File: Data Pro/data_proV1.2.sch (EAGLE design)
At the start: 43 parts, among them IC1 4049N, IC2 MCP3008, IC3 OP11S, IC6 AT24CP, J1 RASPBERRYPI-40-PIN-GPIO, U1 DS18B20, X1 32.768khz

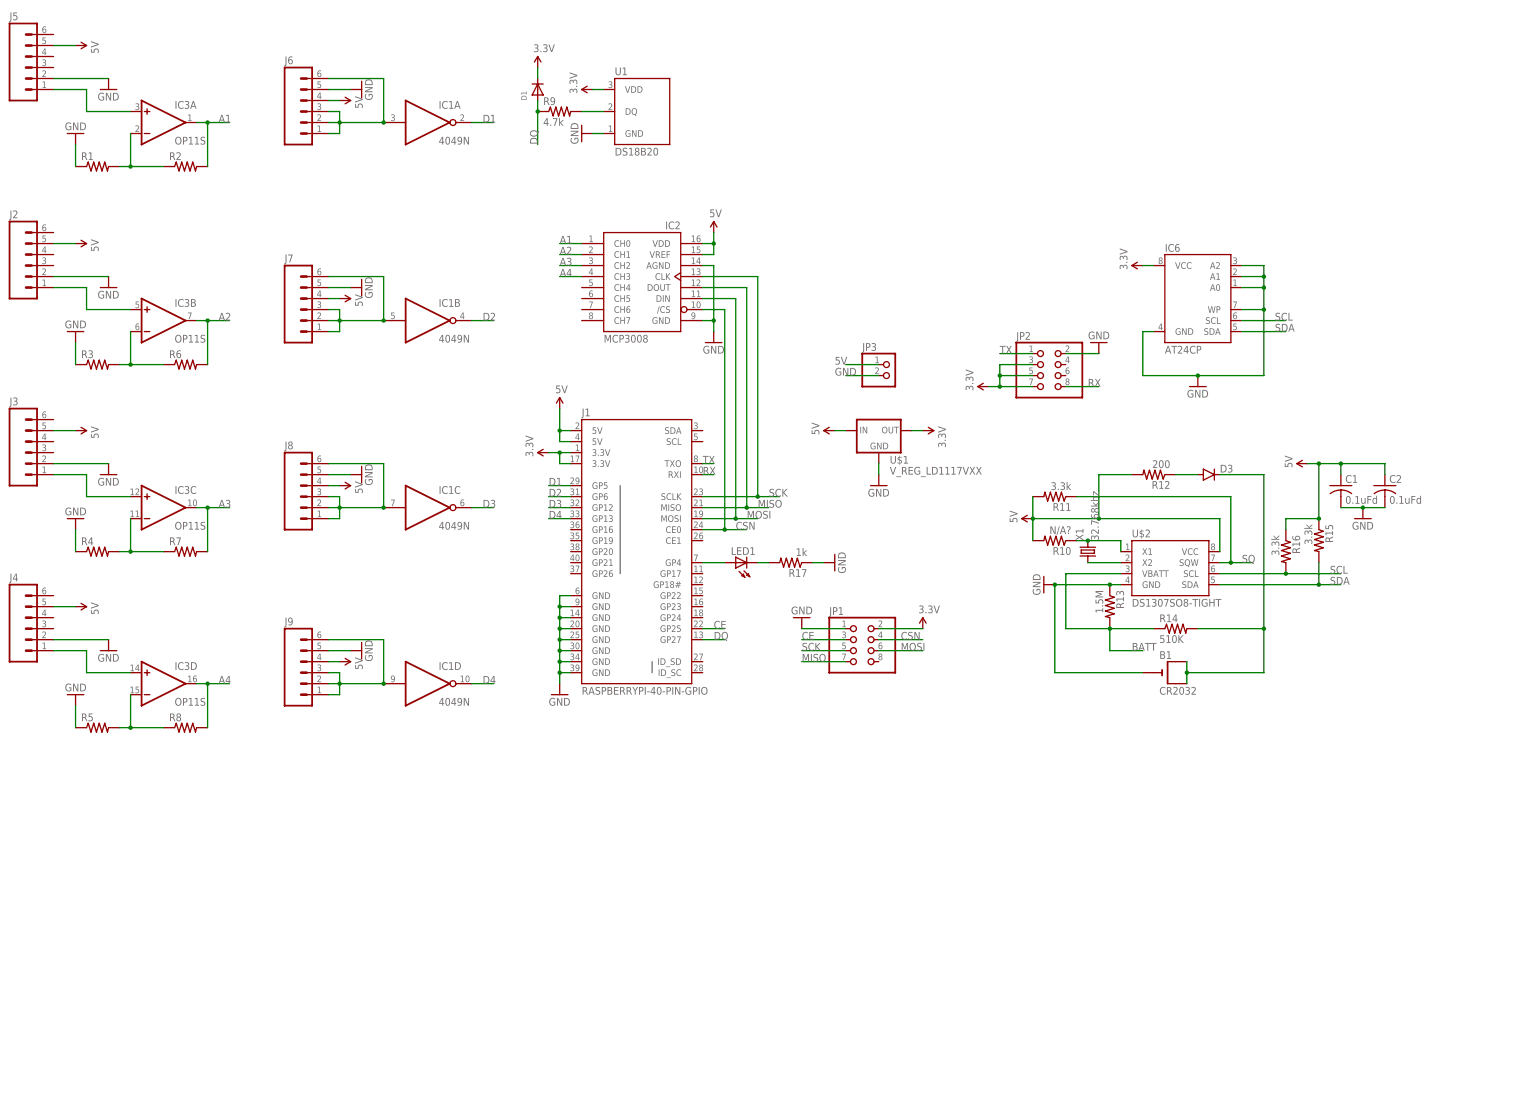
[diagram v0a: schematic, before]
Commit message: Data pro update v1.2
The schematic is complete, working on the board.
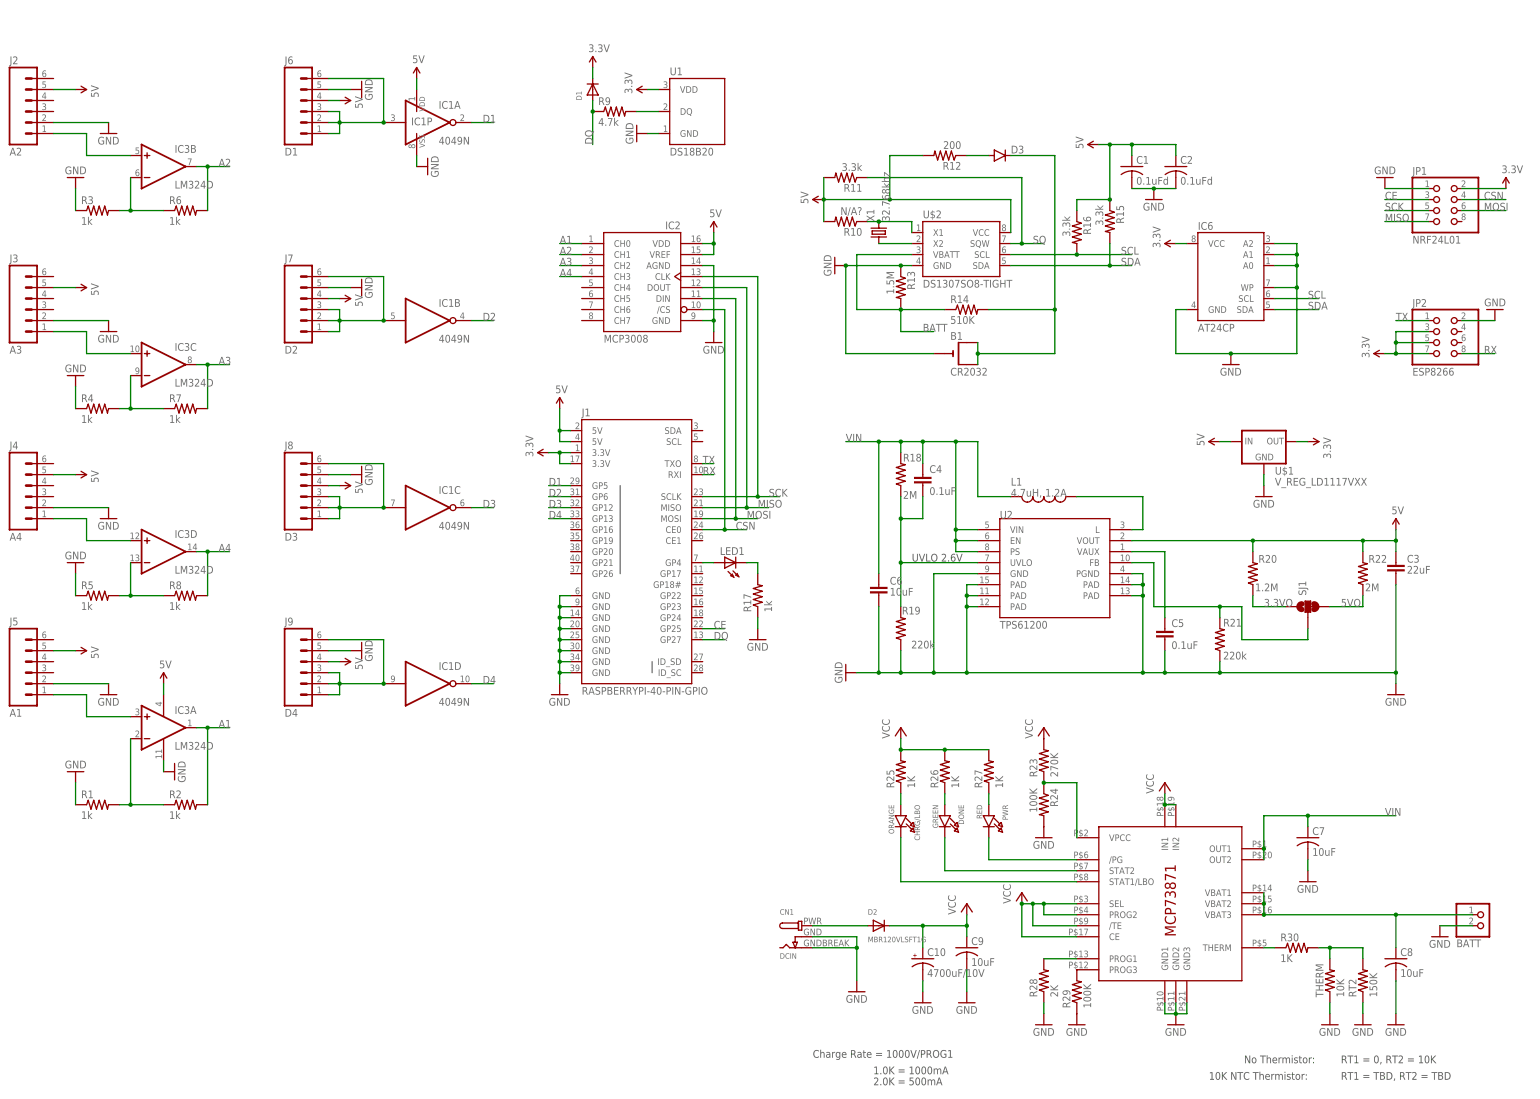
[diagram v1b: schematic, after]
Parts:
- removed JP3: (no value), pinhead:PINHD-1X2
- added BATT: (no value), adafruit:JST_2PIN-SMT-RA
- added C10: 4700uF/10V, adafruit:CPOL-USE5-13
- added C3: 22uF, CH_passive:CAP0805
- added C4, C5: 0.1uF, SparkFun:CAP0603-CAP
- added C6: 10uF, CH_passive:CAP1206
- added C7, C8, C9: 10uF, adafruit:C-USC0805K
- added CHRG/LBO: ORANGE, microbuilder:LED0805_NOOUTLINE
- added CN1: DCIN, microbuilder:DCBARRELSMT
- added D2: MBR120VLSFT1G, microbuilder:DIODESOD-123
- added DONE: GREEN, microbuilder:LED0805_NOOUTLINE
- added IC4: MCP73871, adafruit:MCP73871
- added L1: 4.7uH, 1.2A, SparkFun:INDUCTOR.
- added PWR: RED, microbuilder:LED0805_NOOUTLINE
- added R18, R22: 2M, SparkFun:RESISTOR0603-RES
- added R19, R21: 220k, SparkFun:RESISTOR0603-RES
- added R20: 1.2M, SparkFun:RESISTOR0603-RES
- added R23: 270K, adafruit:R-US_R0805
- added R24, R29: 100K, adafruit:R-US_R0805
- added R25, R26, R27: 1K, adafruit:R-US_R0805
- added R28: 2K, adafruit:R-US_FLIPFLOP
- added R30: 1K, adafruit:R-US_M0805
- added RT2: 150K, adafruit:R-US_M0805
- added SJ1: (no value), SparkFun:SOLDERJUMPER_2WAYPASTE2&3
- added THERM: 10K, adafruit:R-US_FLIPFLOP
- added U2: TPS61200, SparkFun:TPS61200
- IC3: value OP11S -> LM324D; device linear:OP11S -> linear:LM324D
- J2: value (none) -> A2
- J3: value (none) -> A3
- J4: value (none) -> A4
- J5: value (none) -> A1
- J6: value (none) -> D1
- J7: value (none) -> D2
- J8: value (none) -> D3
- J9: value (none) -> D4
- JP1: value (none) -> NRF24L01
- JP2: value (none) -> ESP8266
- R1, R2, R3, R4, R5, R6, R7, R8: value (none) -> 1k
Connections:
- new net 3.3VO: R20.1, SJ1.1
- new net 5VO: R22.1, SJ1.3
- new net BATT1: BATT.2, C8.1, IC4.VBAT1, IC4.VBAT2, IC4.VBAT3
- new net FB: R21.2, SJ1.2, U2.FB
- new net N$13: C5.1, U2.VAUX
- new net N$18: IC4.VPCC, R23.1, R24.1
- new net N$19: IC4./PG, PWR.C
- new net N$20: DONE.C, IC4.STAT2
- new net N$21: CHRG/LBO.C, IC4.STAT1/LBO
- new net N$22: CHRG/LBO.A, R25.1
- new net N$23: DONE.A, R26.1
- new net N$24: PWR.A, R27.1
- new net N$25: IC4.PROG3, R29.2
- new net N$26: IC4.PROG1, R28.2
- new net N$27: IC4.THERM, R30.1
- new net N$28: R30.2, RT2.2, THERM.2
- new net N$29: CN1.PWR, D2.A
- new net N$9: L1.1, U2.L
- new net UVLO: C4.2, R18.1, R19.2, U2.UVLO
- new net VCC: C10.+, C9.1, D2.C, IC4./TE, IC4.CE, IC4.IN1, IC4.IN2, IC4.PROG2, IC4.SEL, R23.2, R25.2, R26.2, R27.2
- new net VIN: C4.1, C6.1, C7.1, IC4.OUT1, IC4.OUT2, L1.2, R18.2, U2.EN, U2.PS, U2.VIN
- net 5V: now also C3.1, IC1P.VDD, IC3P.V+, R20.2, R22.2, U2.VOUT; no longer JP3.1
- net GND: now also BATT.1, C10.-, C3.2, C5.2, C6.2, C7.2, C8.2, C9.2, CN1.GND, CN1.GNDBREAK, IC1P.VSS, IC3P.V-, IC4.GND1, IC4.GND2, IC4.GND3, R19.1, R21.1, R24.2, R28.1, R29.1, RT2.1, THERM.1, U2.GND, U2.PAD@1, U2.PAD@2, U2.PAD@3, U2.PAD@4, U2.PAD@5, U2.PGND; no longer JP3.2
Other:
- note added: "1.0K = 1000mA"
- note added: "10K NTC Thermistor:"
- note added: "2.0K = 500mA"
- note added: "Charge Rate = 1000V/PROG1"
- note added: "No Thermistor:"
- note added: "RT1 = 0, RT2 = 10K"
- note added: "RT1 = TBD, RT2 = TBD"
- note added: "UVLO 2.6V"
- moved on the sheet: B1, C1, C2, D1, D3, IC3A, IC3B, IC3C, IC3D, IC6, J2, J3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

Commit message: Data pro complete
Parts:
- removed JP1: NRF24L01, pinhead:PINHD-2X4
- added M1: WIRELESS-NRF24L01, diy-modules:WIRELESS-NRF24L01
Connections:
- net 3.3V: now also M1.VCC; no longer JP1.2
- net CE: now also M1.CE; no longer JP1.3
- net CSN: now also M1.CSN; no longer JP1.4
- net GND: now also M1.GND; no longer JP1.1
- net MISO: now also M1.MISO; no longer JP1.7
- net MOSI: now also M1.MOSI; no longer JP1.6
- net SCK: now also M1.SCK; no longer JP1.5
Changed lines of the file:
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@@
 <part name="GND17" library="SparkFun-Aesthetics" deviceset="GND" device=""/>
 <part name="SUPPLY14" library="SparkFun-Aesthetics" deviceset="3.3V" device=""/>
-<part name="JP1" library="pinhead" deviceset="PINHD-2X4" device="" value="NRF24L01"/>
-<part name="GND18" library="SparkFun-Aesthetics" deviceset="GND" device=""/>
-<part name="SUPPLY15" library="SparkFun-Aesthetics" deviceset="3.3V" device=""/>
 <part name="U1" library="SparkFun-Sensors" deviceset="DS18B20" device=""/>
 <part name="SUPPLY16" library="SparkFun-Aesthetics" deviceset="3.3V" device=""/>
@@
 <part name="THERM" library="adafruit" deviceset="R-US_" device="FLIPFLOP" value="10K"/>
 <part name="GND39" library="SparkFun" deviceset="GND" device=""/>
+<part name="M1" library="diy-modules" deviceset="WIRELESS-NRF24L01" device=""/>
+<part name="SUPPLY24" library="SparkFun-Aesthetics" deviceset="3.3V" device=""/>
+<part name="GND31" library="SparkFun-Aesthetics" deviceset="GND" device=""/>
 </parts>
 <sheets>
@@
 <instance part="GND17" gate="1" x="259.08" y="76.2"/>
 <instance part="SUPPLY14" gate="G$1" x="269.24" y="88.9" rot="R270"/>
-<instance part="JP1" gate="A" x="299.72" y="142.24"/>
-<instance part="GND18" gate="1" x="287.02" y="149.86" rot="R180"/>
-<instance part="SUPPLY15" gate="G$1" x="314.96" y="147.32"/>
 <instance part="U1" gate="G$1" x="129.54" y="162.56"/>
 <instance part="SUPPLY16" gate="G$1" x="116.84" y="170.18" rot="R90"/>
@@
 <instance part="THERM" gate="G$1" x="274.32" y="-35.56" rot="R90"/>
 <instance part="GND39" gate="1" x="162.56" y="35.56" rot="R270"/>
+<instance part="M1" gate="G$1" x="309.88" y="139.7"/>
+<instance part="SUPPLY24" gate="G$1" x="281.94" y="147.32" rot="R90"/>
+<instance part="GND31" gate="1" x="281.94" y="152.4" rot="R180"/>
 </instances>
 <busses>
@@
 <wire x1="-15.24" y1="53.34" x2="-15.24" y2="58.42" width="0.1524" layer="91"/>
 <pinref part="GND10" gate="1" pin="GND"/>
-</segment>
-<segment>
-<pinref part="JP1" gate="A" pin="1"/>
-<wire x1="297.18" y1="147.32" x2="287.02" y2="147.32" width="0.1524" layer="91"/>
-<pinref part="GND18" gate="1" pin="GND"/>
 </segment>
 <segment>
@@
 <pinref part="THERM" gate="G$1" pin="1"/>
 </segment>
+<segment>
+<pinref part="M1" gate="G$1" pin="GND"/>
+<wire x1="287.02" y1="149.86" x2="281.94" y2="149.86" width="0.1524" layer="91"/>
+<pinref part="GND31" gate="1" pin="GND"/>
+</segment>
 </net>
 <net name="3.3V" class="0">
@@
 <pinref part="U$1" gate="G$1" pin="OUT"/>
 <wire x1="269.24" y1="88.9" x2="266.7" y2="88.9" width="0.1524" layer="91"/>
-</segment>
-<segment>
-<pinref part="JP1" gate="A" pin="2"/>
-<wire x1="304.8" y1="147.32" x2="314.96" y2="147.32" width="0.1524" layer="91"/>
-<pinref part="SUPPLY15" gate="G$1" pin="3.3V"/>
 </segment>
 <segment>
@@
 <junction x="289.56" y="111.76"/>
 <junction x="289.56" y="109.22"/>
+</segment>
+<segment>
+<pinref part="M1" gate="G$1" pin="VCC"/>
+<wire x1="287.02" y1="147.32" x2="281.94" y2="147.32" width="0.1524" layer="91"/>
+<pinref part="SUPPLY24" gate="G$1" pin="3.3V"/>
 </segment>
 </net>
@@
 <net name="MOSI" class="0">
 <segment>
-<pinref part="JP1" gate="A" pin="6"/>
-<wire x1="304.8" y1="142.24" x2="314.96" y2="142.24" width="0.1524" layer="91"/>
-<label x="309.88" y="142.24" size="1.778" layer="95"/>
-</segment>
-<segment>
 <pinref part="IC2" gate="G$1" pin="DIN"/>
 <wire x1="129.54" y1="121.92" x2="137.16" y2="121.92" width="0.1524" layer="91"/>
@@
 <junction x="137.16" y="71.12"/>
 </segment>
+<segment>
+<pinref part="M1" gate="G$1" pin="MOSI"/>
+<wire x1="287.02" y1="137.16" x2="281.94" y2="137.16" width="0.1524" layer="91"/>
+<label x="281.94" y="137.16" size="1.778" layer="95"/>
+</segment>
 </net>
 <net name="CSN" class="0">
-<segment>
-<pinref part="JP1" gate="A" pin="4"/>
-<wire x1="304.8" y1="144.78" x2="314.96" y2="144.78" width="0.1524" layer="91"/>
-<label x="309.88" y="144.78" size="1.778" layer="95"/>
-</segment>
 <segment>
 <pinref part="IC2" gate="G$1" pin="/CS"/>
@@
 <label x="137.16" y="68.58" size="1.778" layer="95"/>
 </segment>
+<segment>
+<pinref part="M1" gate="G$1" pin="CSN"/>
+<wire x1="287.02" y1="142.24" x2="281.94" y2="142.24" width="0.1524" layer="91"/>
+<label x="281.94" y="142.24" size="1.778" layer="95"/>
+</segment>
 </net>
 <net name="CE" class="0">
-<segment>
-<pinref part="JP1" gate="A" pin="3"/>
-<wire x1="297.18" y1="144.78" x2="287.02" y2="144.78" width="0.1524" layer="91"/>
-<label x="287.02" y="144.78" size="1.778" layer="95"/>
-</segment>
 <segment>
 <pinref part="J1" gate="G$1" pin="GP25"/>
 <wire x1="129.54" y1="45.72" x2="134.62" y2="45.72" width="0.1524" layer="91"/>
 <label x="132.08" y="45.72" size="1.778" layer="95"/>
+</segment>
+<segment>
+<pinref part="M1" gate="G$1" pin="CE"/>
+<wire x1="287.02" y1="144.78" x2="281.94" y2="144.78" width="0.1524" layer="91"/>
+<label x="281.94" y="144.78" size="1.778" layer="95"/>
 </segment>
 </net>
@@
 </net>
 <net name="SCK" class="0">
-<segment>
-<pinref part="JP1" gate="A" pin="5"/>
-<wire x1="297.18" y1="142.24" x2="287.02" y2="142.24" width="0.1524" layer="91"/>
-<label x="287.02" y="142.24" size="1.778" layer="95"/>
-</segment>
 <segment>
 <pinref part="IC2" gate="G$1" pin="CLK"/>
@@
 <junction x="142.24" y="76.2"/>
 </segment>
+<segment>
+<pinref part="M1" gate="G$1" pin="SCK"/>
+<wire x1="287.02" y1="139.7" x2="281.94" y2="139.7" width="0.1524" layer="91"/>
+<label x="281.94" y="139.7" size="1.778" layer="95"/>
+</segment>
 </net>
 <net name="MISO" class="0">
-<segment>
-<pinref part="JP1" gate="A" pin="7"/>
-<wire x1="297.18" y1="139.7" x2="287.02" y2="139.7" width="0.1524" layer="91"/>
-<label x="287.02" y="139.7" size="1.778" layer="95"/>
-</segment>
 <segment>
 <pinref part="IC2" gate="G$1" pin="DOUT"/>
@@
 <junction x="139.7" y="73.66"/>
 </segment>
-</net>
+<segment>
+<pinref part="M1" gate="G$1" pin="MISO"/>
+<wire x1="287.02" y1="134.62" x2="281.94" y2="134.62" width="0.1524" layer="91"/>
+<label x="281.94" y="134.62" size="1.778" layer="95"/>
+</segment>
+</net>

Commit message: More data pro updates
Sorry
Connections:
- net CE: now also J1.GP22; no longer J1.GP25
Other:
- moved on the sheet: IC1P
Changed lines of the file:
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@@
 </instance>
 <instance part="IC3" gate="P" x="5.08" y="22.86"/>
-<instance part="IC1" gate="P" x="63.5" y="162.56"/>
+<instance part="IC1" gate="P" x="66.04" y="162.56"/>
 <instance part="SUPPLY21" gate="G$1" x="5.08" y="33.02"/>
 <instance part="GND16" gate="1" x="7.62" y="12.7" rot="R90"/>
-<instance part="GND25" gate="1" x="66.04" y="152.4" rot="R90"/>
-<instance part="SUPPLY22" gate="G$1" x="63.5" y="172.72"/>
+<instance part="GND25" gate="1" x="66.04" y="149.86"/>
+<instance part="SUPPLY22" gate="G$1" x="66.04" y="172.72"/>
 <instance part="SUPPLY23" gate="G$1" x="289.56" y="68.58"/>
 <instance part="IC4" gate="G$1" x="236.22" y="-17.78"/>
@@
 <pinref part="IC1" gate="P" pin="VDD"/>
 <pinref part="SUPPLY22" gate="G$1" pin="5V"/>
-<wire x1="63.5" y1="172.72" x2="63.5" y2="170.18" width="0.1524" layer="91"/>
+<wire x1="66.04" y1="172.72" x2="66.04" y2="170.18" width="0.1524" layer="91"/>
 </segment>
 <segment>
@@
 <pinref part="IC1" gate="P" pin="VSS"/>
 <pinref part="GND25" gate="1" pin="GND"/>
-<wire x1="63.5" y1="152.4" x2="63.5" y2="154.94" width="0.1524" layer="91"/>
+<wire x1="66.04" y1="152.4" x2="66.04" y2="154.94" width="0.1524" layer="91"/>
 </segment>
 <segment>
@@
 <net name="CE" class="0">
 <segment>
-<pinref part="J1" gate="G$1" pin="GP25"/>
-<wire x1="129.54" y1="45.72" x2="134.62" y2="45.72" width="0.1524" layer="91"/>
-<label x="132.08" y="45.72" size="1.778" layer="95"/>
-</segment>
-<segment>
 <pinref part="M1" gate="G$1" pin="CE"/>
 <wire x1="287.02" y1="144.78" x2="281.94" y2="144.78" width="0.1524" layer="91"/>
 <label x="281.94" y="144.78" size="1.778" layer="95"/>
 </segment>
-</net>
+<segment>
+<pinref part="J1" gate="G$1" pin="GP22"/>
+<wire x1="129.54" y1="53.34" x2="134.62" y2="53.34" width="0.1524" layer="91"/>
+<label x="132.08" y="53.34" size="1.778" layer="95"/>
+</segment>
+</net>
